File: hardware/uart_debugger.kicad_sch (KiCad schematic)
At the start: 4 parts, among them Q3 JSM2302, U3 UART_Module

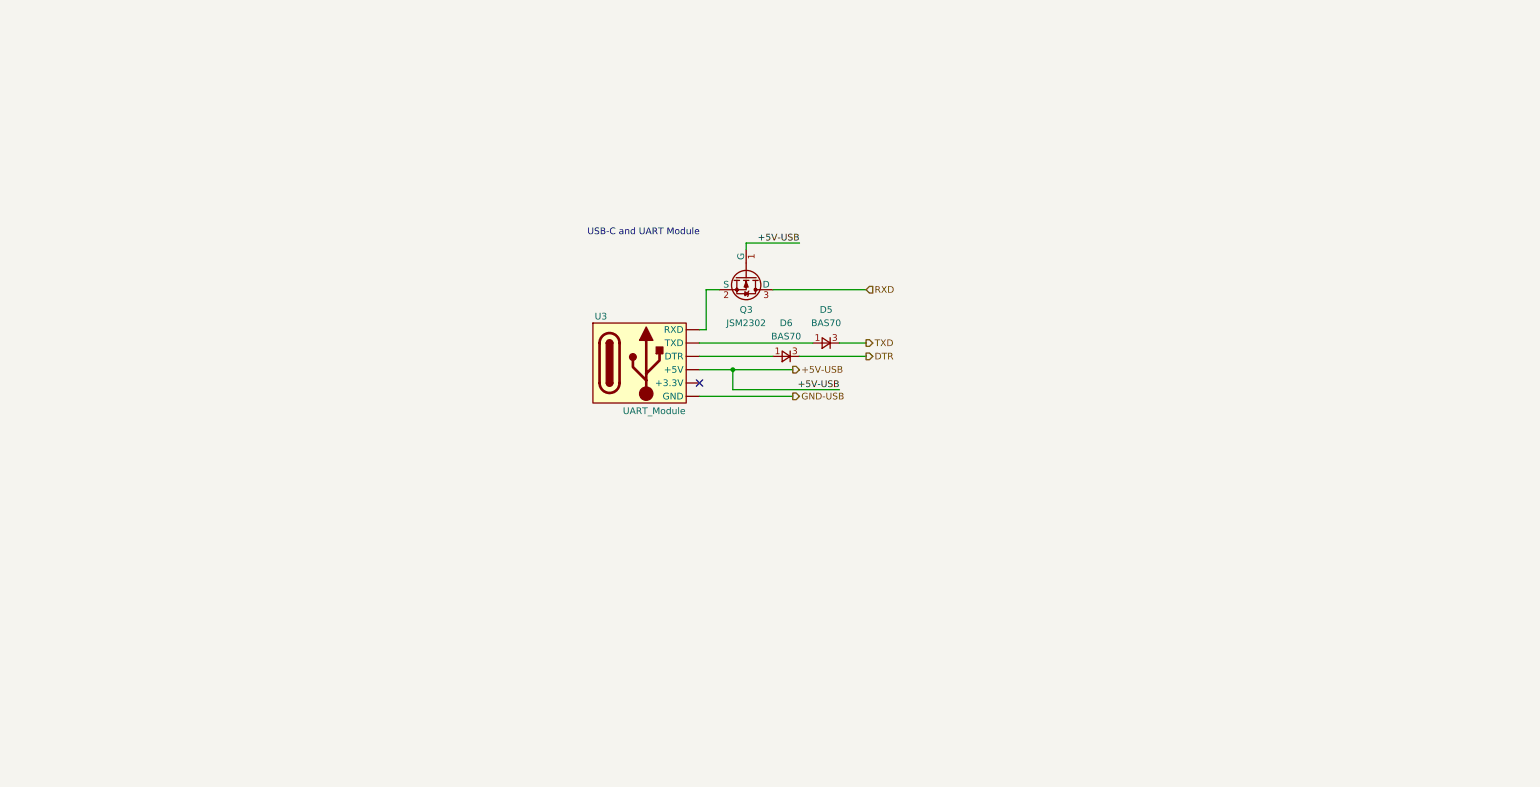
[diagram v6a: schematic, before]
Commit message: Schematic completed, commented and ready for review
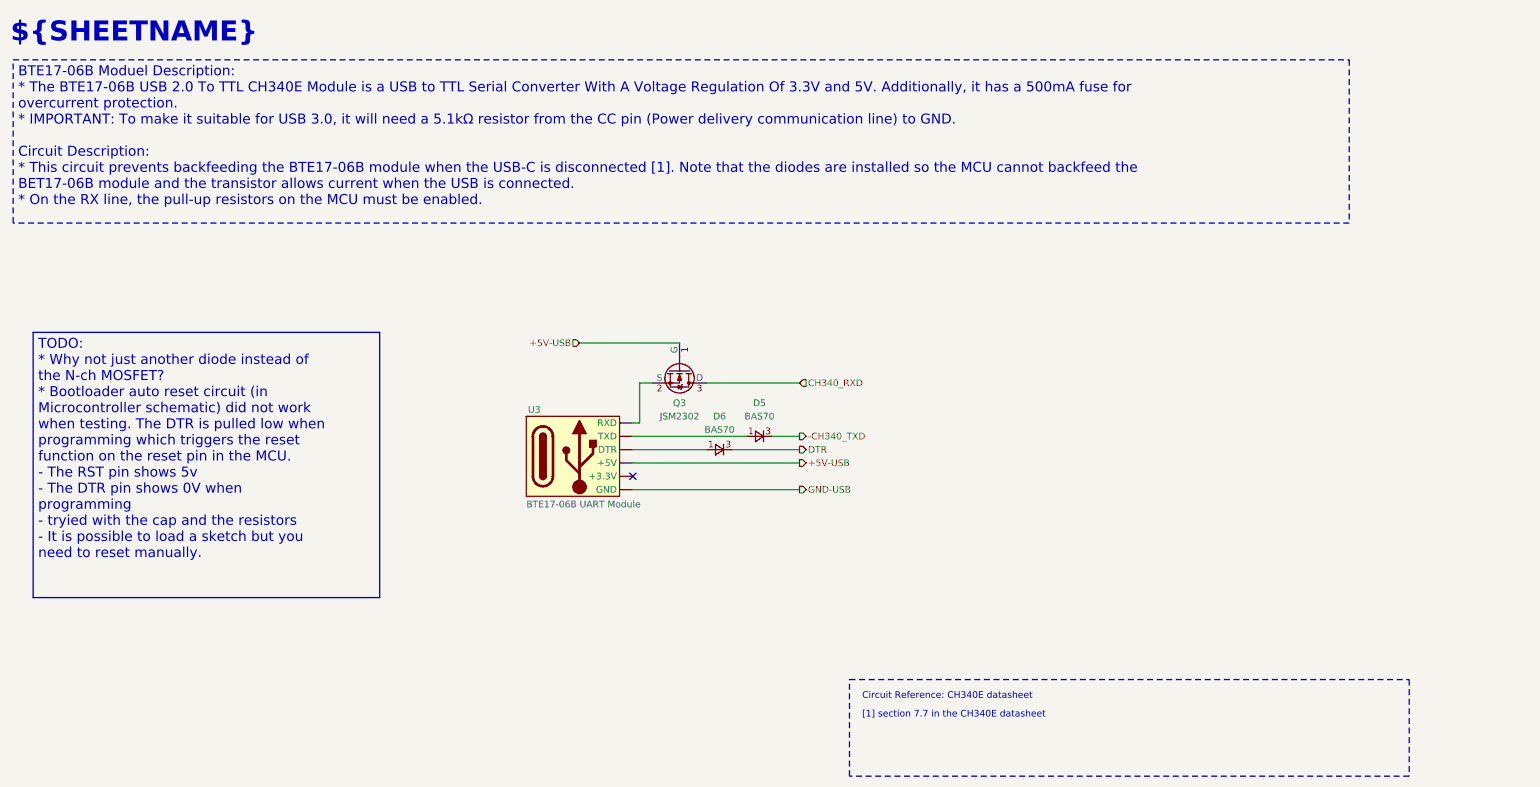
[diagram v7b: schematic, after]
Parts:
- U3: value UART_Module -> BTE17-06B UART Module
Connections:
- net RXD renamed CH340_RXD
- net TXD renamed ­CH340_TXD
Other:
- note added: "${SHEETNAME}"
- note added: "Circuit Reference: CH340E datasheet"
- note added: "[1] section 7.7 in the CH340E datasheet"
- note removed: "USB-C and UART Module"
- title: Kitchen_Timer - USB-C & UART Debugger -> Kitchen_Timer - ${SHEETNAME}
- moved on the sheet: D5, D6, Q3, U3

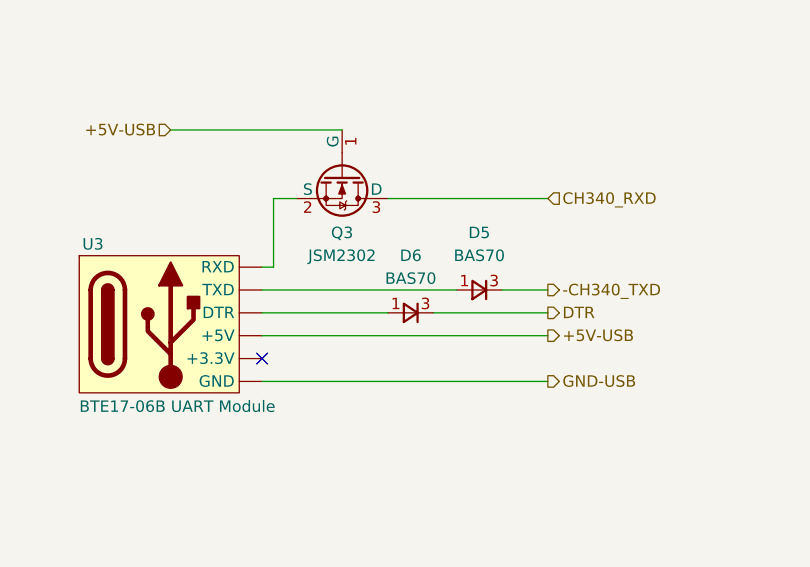
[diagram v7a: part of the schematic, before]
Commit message: Removed diode from the UART block
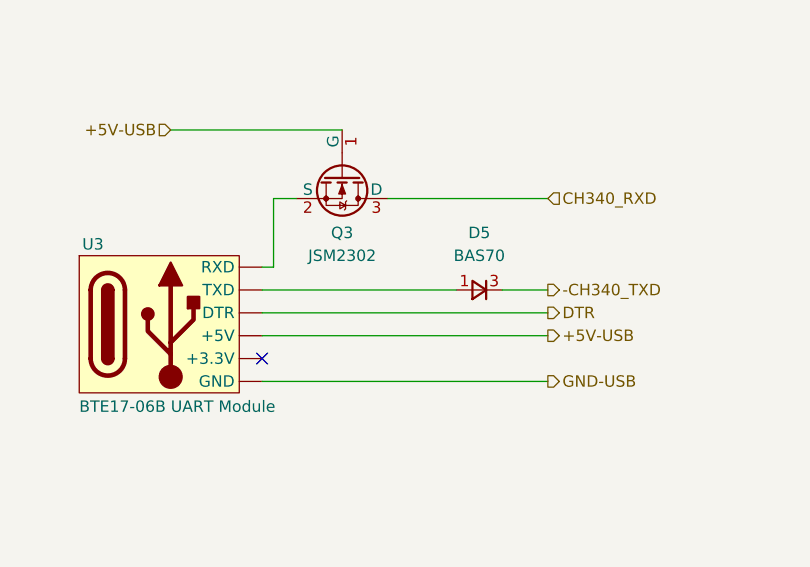
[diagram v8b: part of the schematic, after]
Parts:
- removed D6: BAS70, Package_TO_SOT_SMD:SOT-23, symbol Device:D_Small
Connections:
- net DTR: now also U3. (GND)
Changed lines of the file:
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@@
 	(wire
 		(pts
-			(xy 135.89 102.87) (xy 149.86 102.87)
-		)
-		(stroke
-			(width 0)
-			(type default)
-		)
-	)
-	(wire
-		(pts
-			(xy 154.94 102.87) (xy 167.64 102.87)
+			(xy 135.89 102.87) (xy 167.64 102.87)
 		)
 		(stroke
@@
 		)
 	)
-	(symbol
-		(lib_name "D_Small_1")
-		(lib_id "Device:D_Small")
-		(at 152.4 102.87 0)
-		(mirror y)
-		(unit 1)
-		(exclude_from_sim no)
-		(in_bom yes)
-		(on_board yes)
-		(dnp no)
-		(property "Reference" "D6"
-			(at 152.4 96.52 0)
-			(effects
-				(font
-					(size 1.27 1.27)
-				)
-			)
-		)
-		(property "Value" "BAS70"
-			(at 152.4 99.06 0)
-			(effects
-				(font
-					(size 1.27 1.27)
-				)
-			)
-		)
-		(property "Footprint" "Package_TO_SOT_SMD:SOT-23"
-			(at 131.318 103.124 90)
-			(effects
-				(font
-					(size 1.27 1.27)
-				)
-				(hide yes)
-			)
-		)
-		(property "Datasheet" "https://wmsc.lcsc.com/wmsc/upload/file/pdf/v2/lcsc/2201131400_Yangzhou-Yangjie-Elec-Tech-BAS70_C968045.pdf"
-			(at 135.128 102.108 90)
-			(effects
-				(font
-					(size 1.27 1.27)
-				)
-				(hide yes)
-			)
-		)
-		(property "Description" "70V Independent Type 1V@15mA 70mA SOT-23(TO-236) Schottky Diodes ROHS"
-			(at 151.13 84.328 0)
-			(effects
-				(font
-					(size 1.27 1.27)
-				)
-				(hide yes)
-			)
-		)
-		(property "Sim.Device" "D"
-			(at 160.274 98.298 0)
-			(effects
-				(font
-					(size 1.27 1.27)
-				)
-				(hide yes)
-			)
-		)
-		(property "Sim.Pins" "1=K 2=A"
-			(at 141.224 92.202 0)
-			(effects
-				(font
-					(size 1.27 1.27)
-				)
-				(hide yes)
-			)
-		)
-		(property "Supplier Link" "https://jlcpcb.com/partdetail/Yangzhou_Yangjie_ElecTech-BAS70/C968045"
-			(at 148.59 81.788 0)
-			(effects
-				(font
-					(size 1.27 1.27)
-				)
-				(hide yes)
-			)
-		)
-		(property "Price/unit" "$0.0189"
-			(at 152.146 91.44 0)
-			(effects
-				(font
-					(size 1.27 1.27)
-				)
-				(hide yes)
-			)
-		)
-		(property "Part Num" "BAS70"
-			(at 121.666 90.932 0)
-			(effects
-				(font
-					(size 1.27 1.27)
-				)
-				(hide yes)
-			)
-		)
-		(property "Package" "SOT-23(TO-236)"
-			(at 150.876 87.884 0)
-			(effects
-				(font
-					(size 1.27 1.27)
-				)
-				(hide yes)
-			)
-		)
-		(pin "3"
-		)
-		(pin "1"
-		)
-		(instances
-			(project "kitchen_timer-hardware"
-				(path "/8963deea-96bc-4401-b671-98fbe9ed9c6a/f7e640d9-c0d9-4c44-8592-f18e152ed7d5"
-					(reference "D6")
-					(unit 1)
-				)
-			)
-		)
-	)
